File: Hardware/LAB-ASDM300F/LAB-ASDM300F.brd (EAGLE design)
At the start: 17 x 11.6 mm, 20 parts, among them U1 TPS62240DRVTG4, U2 MIC94325, U3 MAX4377, X1 C-GRID-04-74099, X2 C-GRID-04-74099

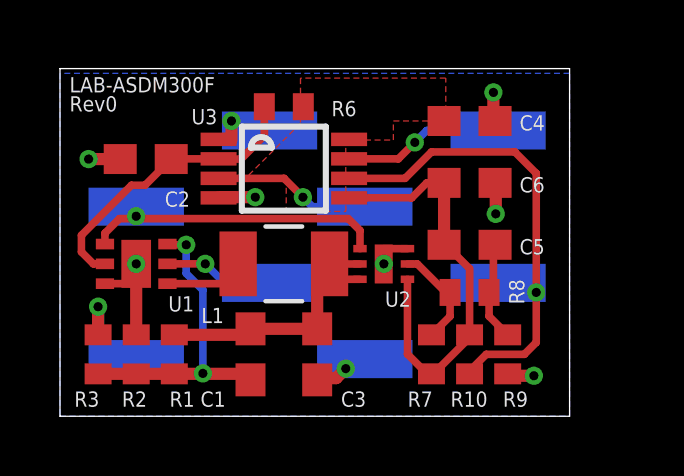
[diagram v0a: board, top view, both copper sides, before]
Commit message: 1) Finished the Rev0 board layout ... but its wrong ... (feedback adjustments are messed up -- fixing now)
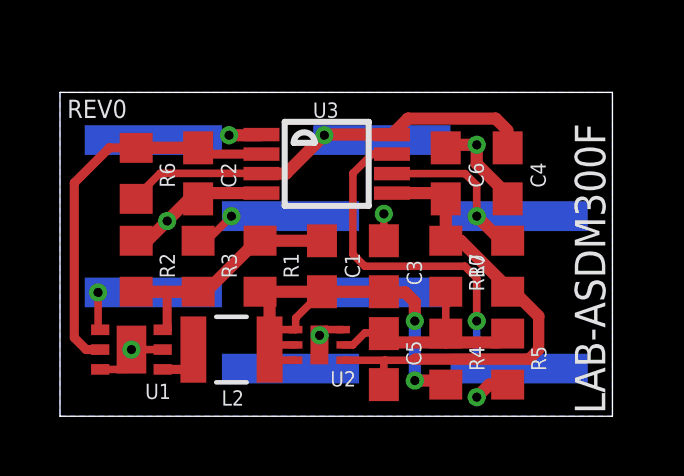
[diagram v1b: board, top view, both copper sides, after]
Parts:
- removed L1: 2.2 uH, Bourns_By_element14_Batch_1:INDC3225X22N
- removed R8, R9: (no value), rcl:R0402
- removed X1, X2: C-GRID-04-74099, con-molex:74099-04
- added J1, J2: SULLINSSMTHEADER-4, LAB-ASDM300F:SMTHEADER-4
- added L2: 2200 nH, Bourns_By_element14_Batch_1:INDC2520X18N
- added R4, R5: (no value), rcl:R0603
- C1: value (none) -> 33pF
- C2, C6: value (none) -> 4.7uF
- C3: value (none) -> 10uF
- C4: value (none) -> .1uF
- C5: value (none) -> 10nF
- R1, R2, R3, R7: device rcl:R0402 -> rcl:R0603
- R10, R6: value (none) -> .1R; device rcl:R0402 -> rcl:R0603
- U3: value MAX4377 -> MAX4377HAUA
- moved R6 5.40 mm to (2.54, 8.10), turned to 90 degrees
- moved C5 4.76 mm to (10.8, 1.91), turned to 90 degrees
- moved R3 4.44 mm to (4.60, 5.00)
- moved R1 4.10 mm to (6.67, 5.00), turned to 270 degrees
- moved C1 3.78 mm to (8.73, 5.00), turned to 90 degrees
- moved C3 3.68 mm to (10.8, 5.00), turned to 90 degrees
- moved U2 3.45 mm to (8.65, 2.38)
- moved R10 3.20 mm to (14.9, 5.00), turned to 270 degrees
- moved R7 2.98 mm to (12.9, 5.00), turned to 90 degrees
- moved R2 2.94 mm to (2.54, 5.00)
- moved U1 2.86 mm to (2.38, 2.22)
- moved C4 2.16 mm to (14.9, 8.10), turned to 270 degrees
- moved C2 1.81 mm to (4.60, 8.10), turned to 270 degrees
- moved U3 1.44 mm to (8.89, 8.41)
- moved C6 0.85 mm to (12.9, 8.10), turned to 90 degrees
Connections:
- removed net BUCKMODE: U1.2, X1.3
- removed net N$2: C1.1, C3.1, L1.2, R1.2, U2.5, U2.6
- removed net PWREN: U1.4, U2.4, X1.2
- new net EN: J1.P$3, U1.4
- net BUCKOUT: now also C1.1, C3.1, L2.1, R1.2, R4.1, U2.4, U2.5, U2.6; no longer C5.2, R8.1, R9.2
- net INCURRENT: now also J1.P$1; no longer X1.1
- net LDOADJ: now also C5.2, R4.2, R5.1; no longer R8.2
- net N$1: now also L2.2; no longer L1.1
- net OUTCURRENT: now also J2.P$1; no longer X2.4
- net PE: now also J1.P$4, J2.P$2, R5.2, U1.2; no longer R9.1, X2.1
- net VADJ: now also J1.P$2; no longer X1.4
- net VIN: now also J2.P$4; no longer X2.3
- net VOUT: now also J2.P$3; no longer X2.2
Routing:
- net BUCKOUT: track 3.43 -> 16.6 mm, vias 0 -> 2
- net VIN: track 5.29 -> 16.5 mm
- net PWREN: track 10.3 -> 0.00 mm, vias 1 -> 0
- net N$2: track 10.1 -> 0.00 mm
- net VOUT: track 16.9 -> 6.80 mm
- net OUTCURRENT: track 5.36 -> 13.2 mm
- net LDOADJ: track 3.48 -> 8.05 mm
- net BUCKMODE: track 3.67 -> 0.00 mm, vias 1 -> 0
- net N$3: track 9.95 -> 13.1 mm
- net EN: track 0.00 -> 3.12 mm, vias 0 -> 1
- net BUCKFB: track 10.3 -> 8.45 mm, vias 2 -> 0
- net N$1: track 3.17 -> 1.67 mm
- net PE: track 12.9 -> 14.3 mm, vias 8 -> 6
- net N$4: track 14.8 -> 16.2 mm
- net INCURRENT: track 3.33 -> 4.00 mm
- removed copper zone on layer 1, net VIN
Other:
- board size 17 x 11.6 mm -> 18.4 x 10.8 mm
- board text added: "REV0"
- board text removed: "Rev0"

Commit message: 1) Revision1 of LAB-ASDM300F 2) Adding ReferenceGuide 3) Removing some autosave crap that should never have been there *) BOM coming soon....
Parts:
- 330K: value (none) -> 360k
- R2: value (none) -> 82k
- R3: value (none) -> 560k
- R4: value (none) -> 220k
- R5: value (none) -> 91k
- R7: value (none) -> 130k
- moved C3 5.16 mm to (14.9, 1.91), turned to 270 degrees
- moved R4 3.72 mm to (10.8, 5.00), turned to 270 degrees
- moved R5 2.06 mm to (12.9, 1.91)
- renumbered R1 to 330K
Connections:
- net BUCKOUT: no longer R4.1
- net VADJ: now also R4.1
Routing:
- net PE: track 14.3 -> 18.7 mm, vias 6 -> 5
- net VADJ: track 3.72 -> 7.02 mm
- net OUTCURRENT: track 13.2 -> 15.9 mm
- net VIN: track 16.5 -> 18.6 mm, vias 1 -> 2
- net BUCKOUT: track 16.6 -> 17.8 mm, vias 2 -> 0
- net LDOADJ: track 8.05 -> 9.16 mm
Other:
- board text added: "REV1"
- board text removed: "REV0"

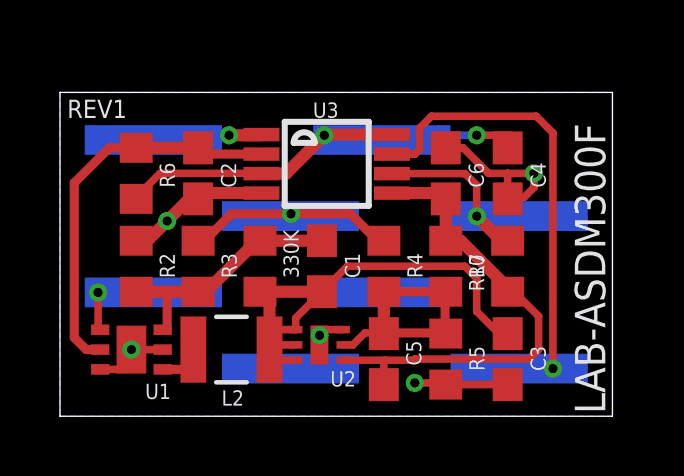
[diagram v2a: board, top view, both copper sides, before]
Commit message: 1) Finished the Rev1 BOM 2) R1 was inadvertently named 330k, changed the designator and bumped the rev. Sticking with Rev2 until new boards go out -- changes may be necessary ...
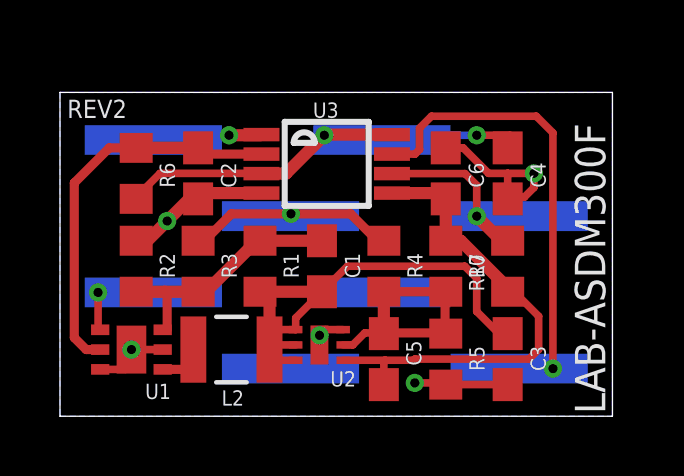
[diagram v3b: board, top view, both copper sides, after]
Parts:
- R1: value 360k -> 330k
- renumbered 330K to R1
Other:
- board text added: "REV2"
- board text removed: "REV1"
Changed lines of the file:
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@@
 <?xml version="1.0" encoding="utf-8"?>
 <!DOCTYPE eagle SYSTEM "eagle.dtd">
-<eagle version="6.5.0">
+<eagle version="6.6.0">
 <drawing>
 <settings>
@@
 <layer number="25" name="tNames" color="7" fill="1" visible="yes" active="yes"/>
 <layer number="26" name="bNames" color="7" fill="1" visible="yes" active="yes"/>
-<layer number="27" name="tValues" color="7" fill="1" visible="no" active="yes"/>
-<layer number="28" name="bValues" color="7" fill="1" visible="no" active="yes"/>
+<layer number="27" name="tValues" color="7" fill="1" visible="yes" active="yes"/>
+<layer number="28" name="bValues" color="7" fill="1" visible="yes" active="yes"/>
 <layer number="29" name="tStop" color="7" fill="3" visible="yes" active="yes"/>
 <layer number="30" name="bStop" color="7" fill="6" visible="yes" active="yes"/>
@@
 <wire x1="0" y1="10.795" x2="0" y2="0" width="0" layer="20"/>
 <text x="18.176875" y="0.079375" size="1.016" layer="21" rot="R90">LAB-ASDM300F</text>
-<text x="0.238125" y="9.94171875" size="0.6096" layer="21">REV1</text>
+<text x="0.238125" y="9.94171875" size="0.6096" layer="21">REV2</text>
 </plain>
 <attributes>
@@
 <attribute name="VALUE" x="5.83565" y="6.0325" size="2.0828" layer="27" ratio="10" rot="SR180"/>
 </element>
-<element name="330K" library="rcl" package="R0603" value="360k" x="6.6675" y="5.000625" smashed="yes" rot="R270">
+<element name="R1" library="rcl" package="R0603" value="330k" x="6.6675" y="5.000625" smashed="yes" rot="R270">
 <attribute name="NAME" x="7.95734375" y="4.60375" size="0.508" layer="25" rot="R90"/>
 <attribute name="VALUE" x="4.7625" y="5.635625" size="1.27" layer="27" rot="R270"/>
@@
 </signal>
 <signal name="BUCKFB">
-<contactref element="330K" pad="1"/>
+<contactref element="R1" pad="1"/>
 <contactref element="R2" pad="2"/>
 <contactref element="C1" pad="2"/>
@@
 </signal>
 <signal name="BUCKOUT">
-<contactref element="330K" pad="2"/>
+<contactref element="R1" pad="2"/>
 <contactref element="U2" pad="6"/>
 <contactref element="U2" pad="5"/>
